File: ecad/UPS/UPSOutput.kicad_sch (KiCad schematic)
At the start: 18 parts, among them U2 MPQ5031GRE-0001-AEC1-P

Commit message: MOSFET and Regulator for output circuit
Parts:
- added D5: 13V, Diode_SMD:D_SMB_Handsoldering, symbol Device:D_Zener
- added Q6: IRLR7843TRPBF, Package_TO_SOT_SMD:TO-252-2, symbol Transistor_FET:Q_NMOS_GDS
- added U3: L78L05_SOT89, Package_TO_SOT_SMD:SOT-89-3, symbol Regulator_Linear:L78L05_SOT89
- D1, D2: footprint Diode_SMD:D_SMB-SMC_Universal_Handsoldering -> Diode_SMD:D_SMB_Handsoldering
- D3, D4: footprint UPS:SOD-962 SL2_TOS -> Diode_SMD:D_SMB_Handsoldering
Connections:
- net +5V: now also U3.1 (OUT)
- net GND: now also D5.2 (A), U3.2 (GND)
- net vbus: now also Q6.3 (S), U3.3 (IN); no longer C11.2, C12.1, U2.20 (VBUS_P), USB_Output1.A4 (VBUS), USB_Output1.A9 (VBUS), USB_Output1.B4 (VBUS), USB_Output1.B9 (VBUS)
- net at U2.19 (VDRV): now also Q6.1 (G)
- new net: C11.2, C12.1, D5.1 (K), Q6.2 (D), U2.20 (VBUS_P), USB_Output1.A4 (VBUS), USB_Output1.A9 (VBUS), USB_Output1.B4 (VBUS), USB_Output1.B9 (VBUS)

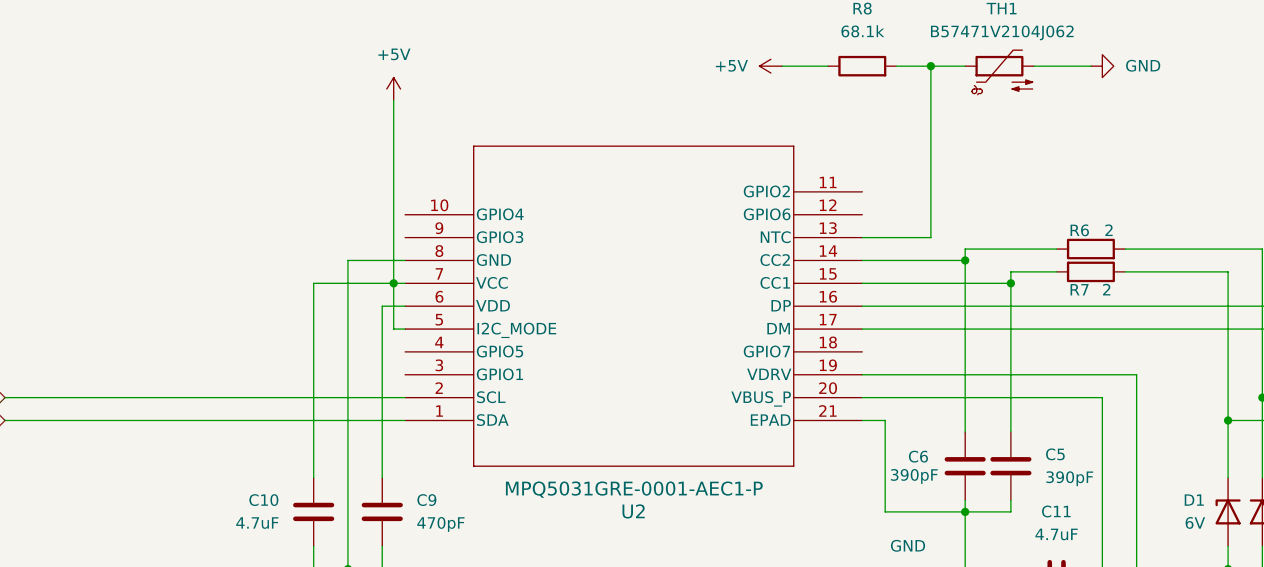
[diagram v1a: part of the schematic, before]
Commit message: Handle PD GPIO pins
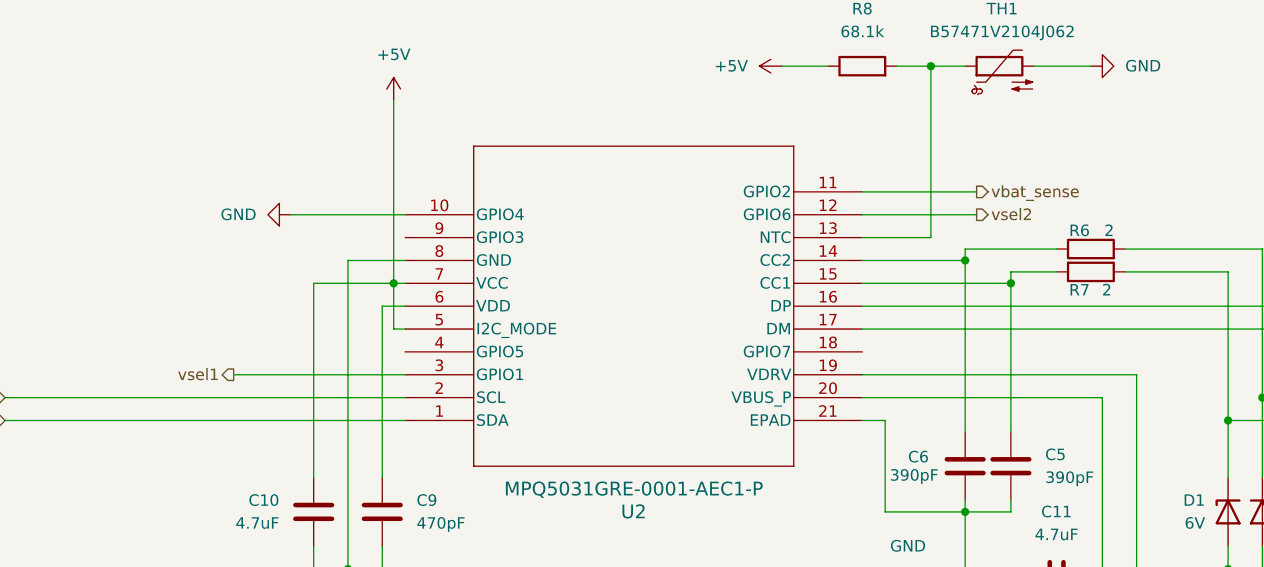
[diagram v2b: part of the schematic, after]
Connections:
- net GND: now also U2.10 (GPIO4)
- net vbat_sense: now reaches U2.11 (GPIO2)
- net vsel2: now reaches U2.12 (GPIO6)
- net vsel1: now reaches U2.3 (GPIO1)
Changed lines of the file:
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@@
 	(wire
 		(pts
+			(xy 54.61 41.91) (xy 67.31 41.91)
+		)
+		(stroke
+			(width 0)
+			(type default)
+		)
+	)
+	(wire
+		(pts
 			(xy 26.67 115.57) (xy 31.75 115.57)
 		)
@@
 	(wire
 		(pts
+			(xy 118.11 41.91) (xy 130.81 41.91)
+		)
+		(stroke
+			(width 0)
+			(type default)
+		)
+	)
+	(wire
+		(pts
 			(xy 118.11 49.53) (xy 134.62 49.53)
 		)
@@
 	(wire
 		(pts
+			(xy 48.26 59.69) (xy 67.31 59.69)
+		)
+		(stroke
+			(width 0)
+			(type default)
+		)
+	)
+	(wire
+		(pts
 			(xy 125.73 44.45) (xy 125.73 25.4)
 		)
@@
 	(wire
 		(pts
+			(xy 118.11 39.37) (xy 130.81 39.37)
+		)
+		(stroke
+			(width 0)
+			(type default)
+		)
+	)
+	(wire
+		(pts
 			(xy 224.79 90.17) (xy 224.79 85.09)
 		)
@@
 		)
 	)
+	(hierarchical_label "vsel2"
+		(shape output)
+		(at 130.81 41.91 0)
+		(effects
+			(font
+				(size 1.27 1.27)
+			)
+			(justify left)
+		)
+	)
 	(hierarchical_label "vbus"
 		(shape input)
@@
 		)
 	)
+	(hierarchical_label "vbat_sense"
+		(shape output)
+		(at 130.81 39.37 0)
+		(effects
+			(font
+				(size 1.27 1.27)
+			)
+			(justify left)
+		)
+	)
+	(hierarchical_label "vsel1"
+		(shape output)
+		(at 48.26 59.69 180)
+		(effects
+			(font
+				(size 1.27 1.27)
+			)
+			(justify right)
+		)
+	)
 	(hierarchical_label "i2c_sda"
 		(shape input)
@@
 					(unit 1)
 				)
+			)
+		)
+	)
+	(symbol
+		(lib_id "power:GND")
+		(at 54.61 41.91 270)
+		(unit 1)
+		(exclude_from_sim no)
+		(in_bom yes)
+		(on_board yes)
+		(dnp no)
+		(fields_autoplaced yes)
+		(property "Reference" "#PWR020"
+			(at 48.26 41.91 0)
+			(effects
+				(font
+					(size 1.27 1.27)
+				)
+				(hide yes)
+			)
+		)
+		(property "Value" "GND"
+			(at 50.8 41.9099 90)
+			(effects
+				(font
+					(size 1.27 1.27)
+				)
+				(justify right)
+			)
+		)
+		(property "Footprint" ""
+			(at 54.61 41.91 0)
+			(effects
+				(font
+					(size 1.27 1.27)
+				)
+				(hide yes)
+			)
+		)
+		(property "Datasheet" ""
+			(at 54.61 41.91 0)
+			(effects
+				(font
+					(size 1.27 1.27)
+				)
+				(hide yes)
+			)
+		)
+		(property "Description" "Power symbol creates a global label with name \"GND\" , ground"
+			(at 54.61 41.91 0)
+			(effects
+				(font
+					(size 1.27 1.27)
+				)
+				(hide yes)
+			)
+		)
+		(pin "1"
+		)
+		(instances
+			(project "UPS"
+				(path "/9d92b60a-4a6b-449c-b462-cab19e69d38c/c2035c51-7de6-43a1-947f-d073f8318def"
+					(reference "#PWR020")
+					(unit 1)
+				)
